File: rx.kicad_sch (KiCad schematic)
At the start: 1 part, among them U1 CC1200

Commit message: Add files via upload
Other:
- moved on the sheet: U1
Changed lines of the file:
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@@
     (comment 1 "Wojciech Kaczmarski, SP5WWP")
   )
-  (symbol (lib_id "RF:CC1200") (at 140.97 91.44 0) (unit 1)
+  (symbol (lib_id "RF:CC1200") (at 190.5 140.97 0) (unit 1)
     (in_bom yes) (on_board yes) (dnp no) (fields_autoplaced)
-    (property "Reference" "U1" (at 140.97 59.3557 0)
+    (property "Reference" "U1" (at 190.5 108.8857 0)
       (effects (font (size 1.27 1.27)))
     )
-    (property "Value" "CC1200" (at 140.97 61.7799 0)
+    (property "Value" "CC1200" (at 190.5 111.3099 0)
       (effects (font (size 1.27 1.27)))
     )
-    (property "Footprint" "Package_DFN_QFN:QFN-32-1EP_5x5mm_P0.5mm_EP3.45x3.45mm" (at 156.21 62.23 0)
+    (property "Footprint" "Package_DFN_QFN:QFN-32-1EP_5x5mm_P0.5mm_EP3.45x3.45mm" (at 205.74 111.76 0)
       (effects (font (size 1.27 1.27)) hide)
     )
-    (property "Datasheet" "http://www.ti.com/lit/ds/symlink/cc1200.pdf" (at 128.27 62.23 0)
+    (property "Datasheet" "http://www.ti.com/lit/ds/symlink/cc1200.pdf" (at 177.8 111.76 0)
       (effects (font (size 1.27 1.27)) hide)
     )
@@
         )
         (path "/4c42207c-9e6b-42da-ad38-da126b892014/67f0dbce-cbd0-480e-94dd-fb4f6a57e3e4"
-          (reference "U9") (unit 1)
+          (reference "U10") (unit 1)
         )
       )

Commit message: Add files via upload
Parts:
- added C5 (x13): 47n, Capacitor_SMD:C_0603_1608Metric, symbol Device:C_Small
- added C5: 1n5, Capacitor_SMD:C_0603_1608Metric, symbol Device:C_Small
- added C5 (x3): 5p1, Capacitor_SMD:C_0603_1608Metric, symbol Device:C_Small
- added C5: 100n, Capacitor_SMD:C_0603_1608Metric, symbol Device:C_Small
- added C5: 6p2, Capacitor_SMD:C_0603_1608Metric, symbol Device:C_Small
- added FB1: Bead, Inductor_SMD:L_0603_1608Metric, symbol Device:FerriteBead_Small
- added L3: 15n, Inductor_SMD:L_0603_1608Metric, symbol Device:L_Small
- added L3 (x2): 27n, Inductor_SMD:L_0603_1608Metric, symbol Device:L_Small
- added L3: 22n, Inductor_SMD:L_0603_1608Metric, symbol Device:L_Small
- added L3: 56n, Inductor_SMD:L_0603_1608Metric, symbol Device:L_Small
- added R2 (x3): 100R, Resistor_SMD:R_0603_1608Metric, symbol Device:R_Small
- added R2: 56k, Resistor_SMD:R_0603_1608Metric, symbol Device:R_Small
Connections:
- net RX_3V3: now reaches U1.1 (VDD_GUARD)
- net RX_3V3: now also U1.12 (DVDD), U1.13 (AVDD_IF), U1.15 (AVDD_RF), U1.17 (PA), U1.22 (AVDD_SYNTH1), U1.25 (AVDD_PFD_CHP), U1.27 (AVDD_SYNTH2), U1.28 (AVDD_XOSC), U1.5 (DVDD), C5.1, C5.1, C5.1, C5.1, C5.1, C5.1, C5.1, C5.1, C5.1, FB1.1
- net SPI_nCS: now reaches U1.11 (~{CS})
- net at U1.14 (RBIAS): now also R2.1
- net at U1.19 (LNA_P): now also C5.1, L3.1, L3.2
- net nRST: now reaches U1.2 (~{RESET})
- net at U1.20 (LNA_N): now also C5.1, L3.1, L3.1
- net at U1.21 (DCPL_VCO): now also C5.1
- net at U1.23 (LPF0): now also C5.1
- net at U1.24 (LPF1): now also C5.2
- net at U1.26 (DCPL_PFD_CHP): now also C5.1
- net at U1.29 (DCPL_XOSC): now also C5.1
- net GND: now reaches U1.33 (GND_EP)
- net GND: now also C5.2, C5.2, C5.2, C5.2, C5.2, C5.2, C5.2, C5.2, C5.2, C5.2, C5.2, C5.2, C5.2, C5.2, C5.2, L3.2, R2.2
- net at U1.6 (DCPL): now also C5.1
- net at U1.7 (SI): now also R2.1
- net at U1.8 (SCLK): now also R2.1
- net at U1.9 (SO(GPIO1)): now also R2.1
- new net: C5.1, L3.1
- new net: C5.2, C5.2, L3.2, L3.2
- new net: C5.1, C5.2, L3.2
- new net 3.3V_IN: C5.1, FB1.2
- new net RF_IN: L3.1
- new net SPI_MISO: R2.2
- new net SPI_MOSI: R2.2
- new net SPI_SCK: R2.2
- no-connect marks 0 -> 6
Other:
- note added: "Decoupling"
- note added: "Receiver"
- moved on the sheet: U1

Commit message: Add files via upload
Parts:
- added JP1: ~, Jumper:SolderJumper-2_P1.3mm_Open_TrianglePad1.0x1.5mm, symbol Jumper:SolderJumper_2_Open
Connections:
- net RX_3V3: now also JP1.1 (A); no longer U1.17 (PA)
- new net: JP1.2 (B), U1.17 (PA)
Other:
- note added: "In case PA needs to be connected to 3.3V"
- note added: "This part might need reworking later"
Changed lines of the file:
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@@
   (junction (at 199.39 71.12) (diameter 0) (color 0 0 0 0)
   )
-  (junction (at 199.39 83.82) (diameter 0) (color 0 0 0 0)
-  )
   (junction (at 177.8 200.66) (diameter 0) (color 0 0 0 0)
   )
@@
   )
   (junction (at 142.24 200.66) (diameter 0) (color 0 0 0 0)
+  )
+  (junction (at 199.39 68.58) (diameter 0) (color 0 0 0 0)
   )
   (no_connect (at 158.75 81.28))
@@
     (stroke (width 0) (type default))
   )
+  (polyline (pts (xy 223.52 115.57) (xy 223.52 121.92))
+    (stroke (width 0) (type dash))
+  )
   (wire (pts (xy 219.71 105.41) (xy 219.71 104.14))
     (stroke (width 0) (type default))
@@
     (stroke (width 0) (type default))
   )
+  (polyline (pts (xy 191.77 115.57) (xy 223.52 115.57))
+    (stroke (width 0) (type dash))
+  )
   (wire (pts (xy 213.36 123.19) (xy 210.82 123.19))
     (stroke (width 0) (type default))
@@
     (stroke (width 0) (type default))
   )
+  (wire (pts (xy 208.28 68.58) (xy 208.28 111.76))
+    (stroke (width 0) (type default))
+  )
   (wire (pts (xy 151.13 200.66) (xy 151.13 203.2))
     (stroke (width 0) (type default))
@@
     (stroke (width 0) (type default))
   )
+  (polyline (pts (xy 191.77 149.86) (xy 191.77 115.57))
+    (stroke (width 0) (type dash))
+  )
   (wire (pts (xy 154.94 68.58) (xy 158.75 68.58))
     (stroke (width 0) (type default))
@@
     (stroke (width 0) (type default))
   )
-  (wire (pts (xy 199.39 111.76) (xy 199.39 83.82))
-    (stroke (width 0) (type default))
-  )
   (wire (pts (xy 168.91 210.82) (xy 168.91 208.28))
     (stroke (width 0) (type default))
@@
     (stroke (width 0) (type default))
   )
+  (wire (pts (xy 200.66 68.58) (xy 199.39 68.58))
+    (stroke (width 0) (type default))
+  )
   (wire (pts (xy 177.8 200.66) (xy 168.91 200.66))
     (stroke (width 0) (type default))
@@
     (stroke (width 0) (type default))
   )
+  (polyline (pts (xy 223.52 121.92) (xy 262.89 121.92))
+    (stroke (width 0) (type dash))
+  )
   (wire (pts (xy 158.75 111.76) (xy 156.21 111.76))
     (stroke (width 0) (type default))
@@
     (stroke (width 0) (type default))
   )
-  (wire (pts (xy 194.31 111.76) (xy 199.39 111.76))
+  (polyline (pts (xy 262.89 149.86) (xy 191.77 149.86))
+    (stroke (width 0) (type dash))
+  )
+  (wire (pts (xy 194.31 111.76) (xy 208.28 111.76))
+    (stroke (width 0) (type default))
+  )
+  (wire (pts (xy 199.39 68.58) (xy 199.39 66.04))
     (stroke (width 0) (type default))
   )
@@
     (stroke (width 0) (type default))
   )
+  (polyline (pts (xy 262.89 121.92) (xy 262.89 149.86))
+    (stroke (width 0) (type dash))
+  )
   (wire (pts (xy 213.36 123.19) (xy 219.71 123.19))
     (stroke (width 0) (type default))
@@
     (stroke (width 0) (type default))
   )
-  (wire (pts (xy 199.39 71.12) (xy 199.39 66.04))
+  (wire (pts (xy 199.39 71.12) (xy 199.39 68.58))
     (stroke (width 0) (type default))
   )
@@
     (effects (font (size 3.81 3.81)) (justify left bottom))
   )
+  (text "This part might need reworking later" (at 224.79 120.65 0)
+    (effects (font (size 1.27 1.27)) (justify left bottom))
+  )
+  (text "In case PA needs to be connected to 3.3V" (at 209.55 69.85 0)
+    (effects (font (size 1.27 1.27)) (justify left bottom))
+  )
   (label "RX_3V3" (at 201.93 60.96 0) (fields_autoplaced)
     (effects (font (size 1.27 1.27)) (justify left bottom))
@@
     )
   )
+  (symbol (lib_id "Jumper:SolderJumper_2_Open") (at 204.47 68.58 0) (unit 1)
+    (in_bom yes) (on_board yes) (dnp no)
+    (property "Reference" "JP1" (at 204.47 66.04 0)
+      (effects (font (size 1.27 1.27)))
+    )
+    (property "Value" "~" (at 204.47 65.9709 0)
+      (effects (font (size 1.27 1.27)))
+    )
+    (property "Footprint" "Jumper:SolderJumper-2_P1.3mm_Open_TrianglePad1.0x1.5mm" (at 204.47 68.58 0)
+      (effects (font (size 1.27 1.27)) hide)
+    )
+    (property "Datasheet" "~" (at 204.47 68.58 0)
+      (effects (font (size 1.27 1.27)) hide)
+    )
+    (pin "1")
+    (pin "2")
+    (instances
+      (project "m17-rru-rf"
+        (path "/4c42207c-9e6b-42da-ad38-da126b892014/67f0dbce-cbd0-480e-94dd-fb4f6a57e3e4"
+          (reference "JP1") (unit 1)
+        )
+      )
+    )
+  )
   (symbol (lib_id "power:GND") (at 242.57 144.78 0) (unit 1)
     (in_bom yes) (on_board yes) (dnp no)
@@
         )
         (path "/4c42207c-9e6b-42da-ad38-da126b892014/67f0dbce-cbd0-480e-94dd-fb4f6a57e3e4"
-          (reference "R27") (unit 1)
+          (reference "R30") (unit 1)
         )
       )
@@
         )
         (path "/4c42207c-9e6b-42da-ad38-da126b892014/67f0dbce-cbd0-480e-94dd-fb4f6a57e3e4"
-          (reference "R28") (unit 1)
+          (reference "R31") (unit 1)
         )
       )
@@
         )
         (path "/4c42207c-9e6b-42da-ad38-da126b892014/67f0dbce-cbd0-480e-94dd-fb4f6a57e3e4"
-          (reference "R29") (unit 1)
+          (reference "R32") (unit 1)
         )
       )
@@
         )
         (path "/4c42207c-9e6b-42da-ad38-da126b892014/67f0dbce-cbd0-480e-94dd-fb4f6a57e3e4"
-          (reference "R26") (unit 1)
-        )
-      )
+          (reference "R29") (unit 1)
+        )
+      )

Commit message: partial PN update
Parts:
- C5: PN (none) -> C0603C473K5RACTU
- C5: PN (none) -> GRM1885C1H152JA01D
- C5: PN (none) -> C0603C104M5RAC7411

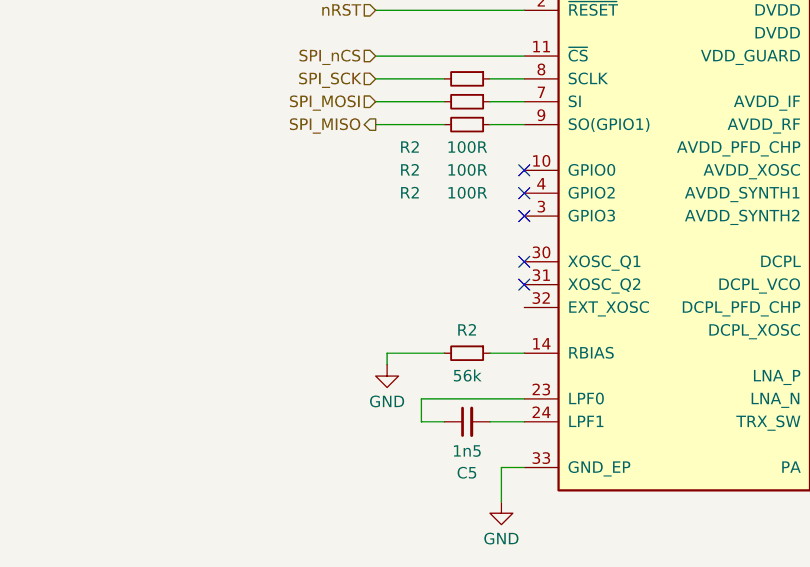
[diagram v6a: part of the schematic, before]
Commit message: added missing 40MHz source
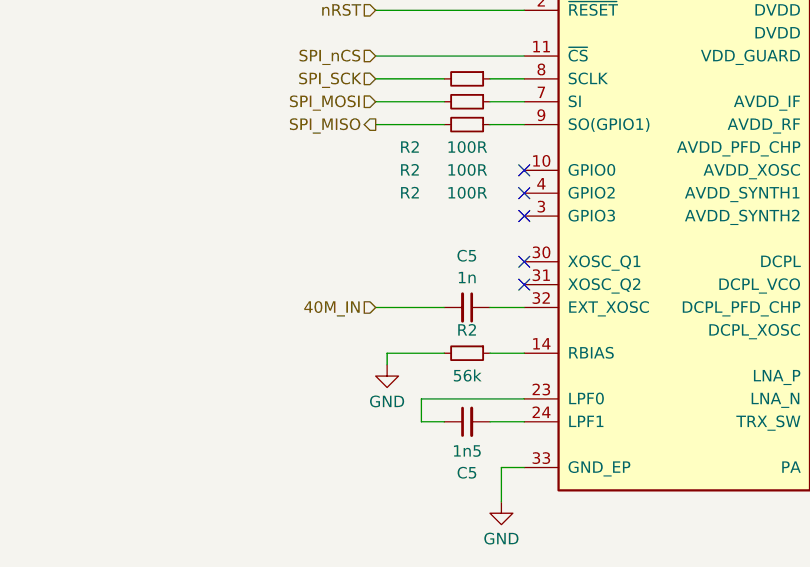
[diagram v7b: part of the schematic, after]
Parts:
- added C5: 1n, Capacitor_SMD:C_0603_1608Metric, symbol Device:C_Small
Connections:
- net at U1.32 (EXT_XOSC): now also C5.1
- new net 40M_IN: C5.2

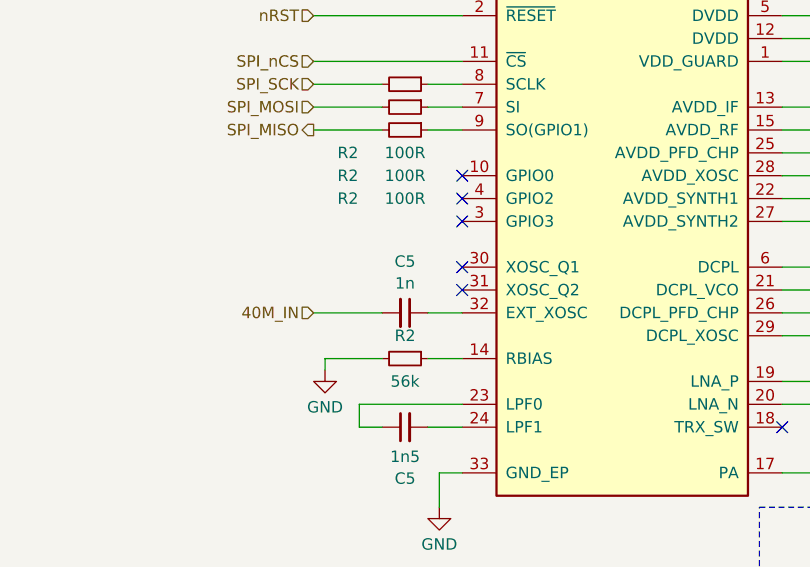
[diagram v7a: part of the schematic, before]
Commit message: caps' val update
40MHz TCXO's max. output load is 10p||10k
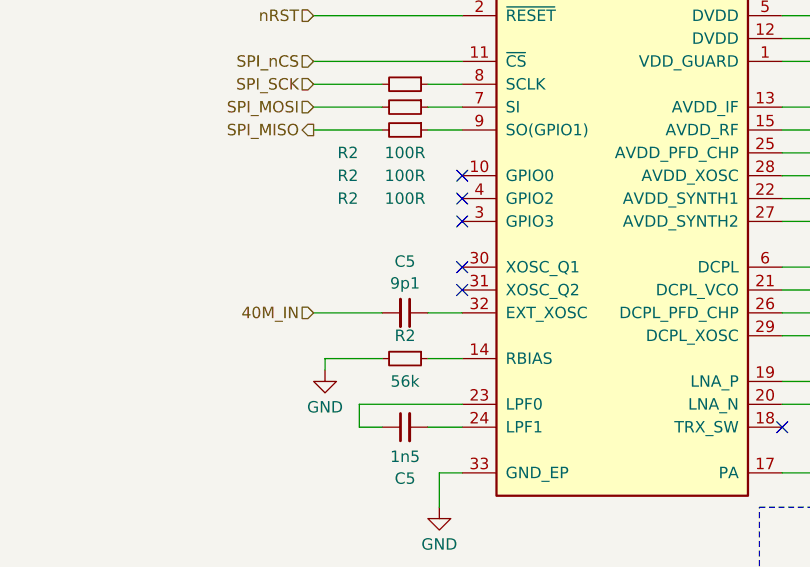
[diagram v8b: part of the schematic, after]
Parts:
- C5: value 1n -> 9p1; PN C0603C102J5GAC7411 -> (none)
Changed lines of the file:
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@@
       (effects (font (size 1.27 1.27)))
     )
-    (property "Value" "1n" (at 152.3937 90.6978 90)
+    (property "Value" "9p1" (at 152.3937 90.6978 90)
       (effects (font (size 1.27 1.27)))
     )
@@
       (effects (font (size 1.27 1.27)) hide)
     )
-    (property "PN" "C0603C102J5GAC7411" (at 152.4 93.98 0)
+    (property "PN" "" (at 152.4 93.98 0)
       (effects (font (size 1.27 1.27)) hide)
     )
